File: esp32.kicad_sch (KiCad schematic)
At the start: 46 parts, among them J4 TC2030-IDC, J5 Conn_01x04, J6 Conn_01x06, J8 USB_C_Receptacle_USB2.0, SW1 SWITCH-SPST, SW2 SWITCH-SPST, U5 SN74AVC4T774, U6 ESP32-S3-WROOM-1, Y1 32.768kHz

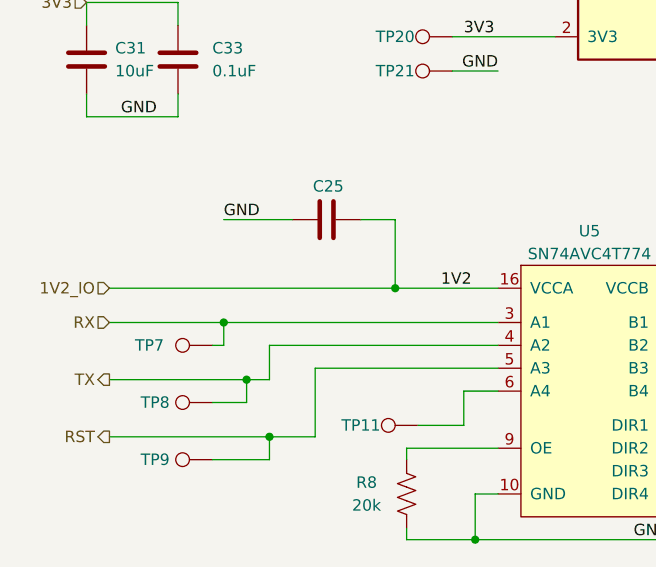
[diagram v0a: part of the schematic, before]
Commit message: -Reset to 1V8/0V8 setup -Add TVS protection
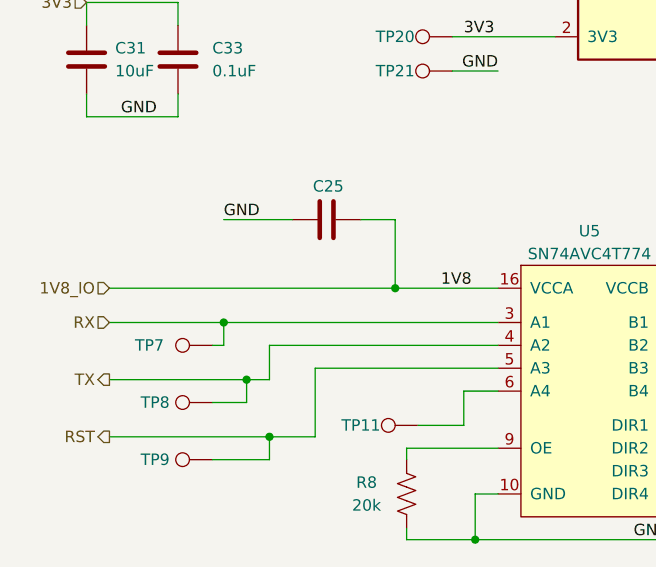
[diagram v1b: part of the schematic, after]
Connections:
- net 1V2_IO renamed 1V8_IO
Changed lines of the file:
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@@
 		)
 	)
-	(label "1V2"
+	(label "1V8"
 		(at 60.96 157.48 0)
 		(fields_autoplaced yes)
@@
 		)
 	)
-	(hierarchical_label "1V2_IO"
+	(hierarchical_label "1V8_IO"
 		(shape input)
 		(at 24.13 157.48 180)

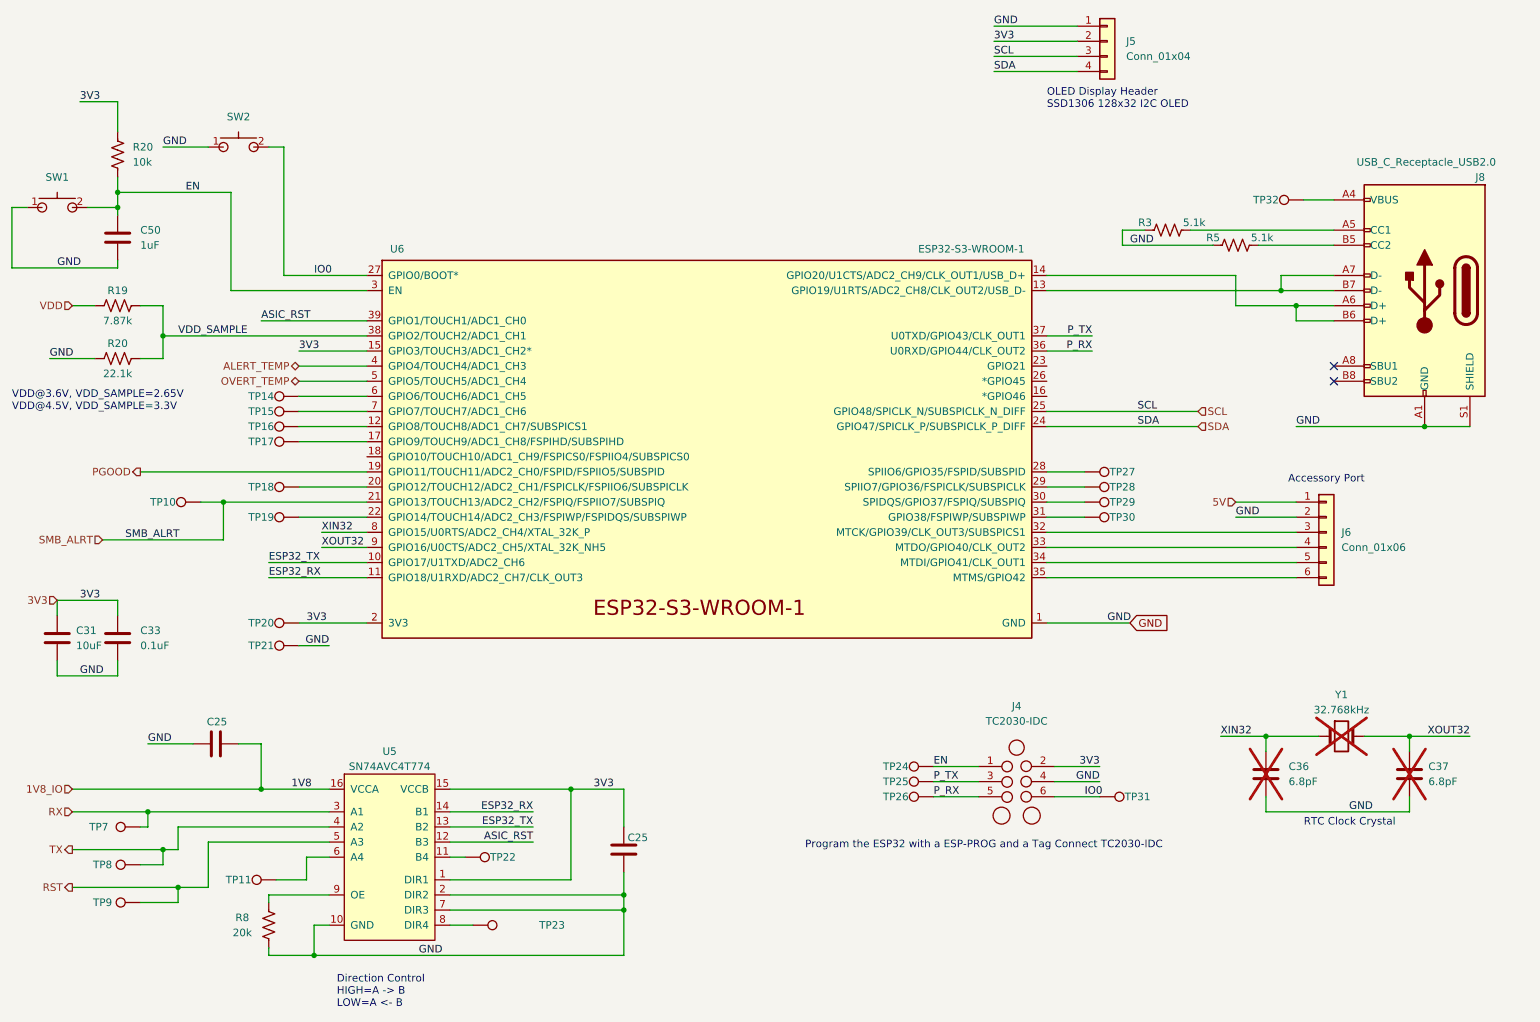
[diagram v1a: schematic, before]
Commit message: updated to KiCad v9, filled in incomplete BOM and exported.
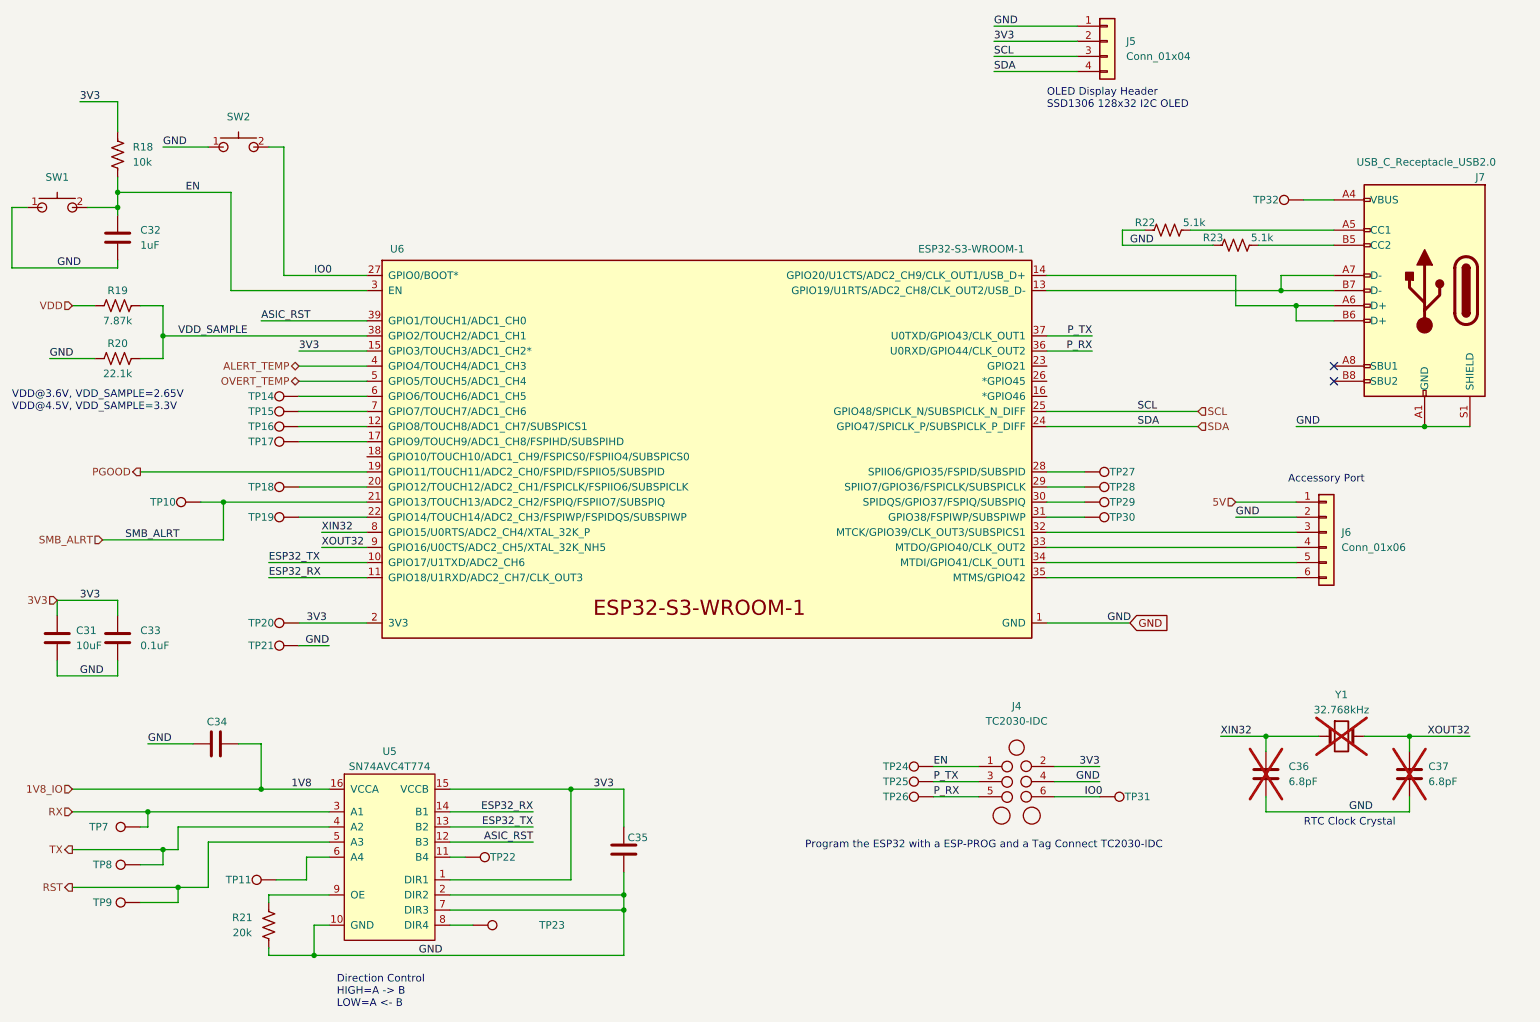
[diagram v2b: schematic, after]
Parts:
- renumbered C50 to C32, C25 to C34, C25 to C35, J8 to J7, R20 to R18, R8 to R21, R3 to R22, R5 to R23
